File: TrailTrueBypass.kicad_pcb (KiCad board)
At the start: 2 copper layers, 38.1 x 22.6 mm, 53 parts, among them J1 Conn_01x05_Pin, J2 Conn_01x05_Pin, J3 Conn_02x03_Top_Bottom, K1 G6S-2, K2 G6S-2, K3 G6S-2, Q1 2N3904, Q2 2N3904, Q3 2N3904, U1 Opamp_Quad, U2 MC78L05_SOT89, U3 PIC12F675-xP

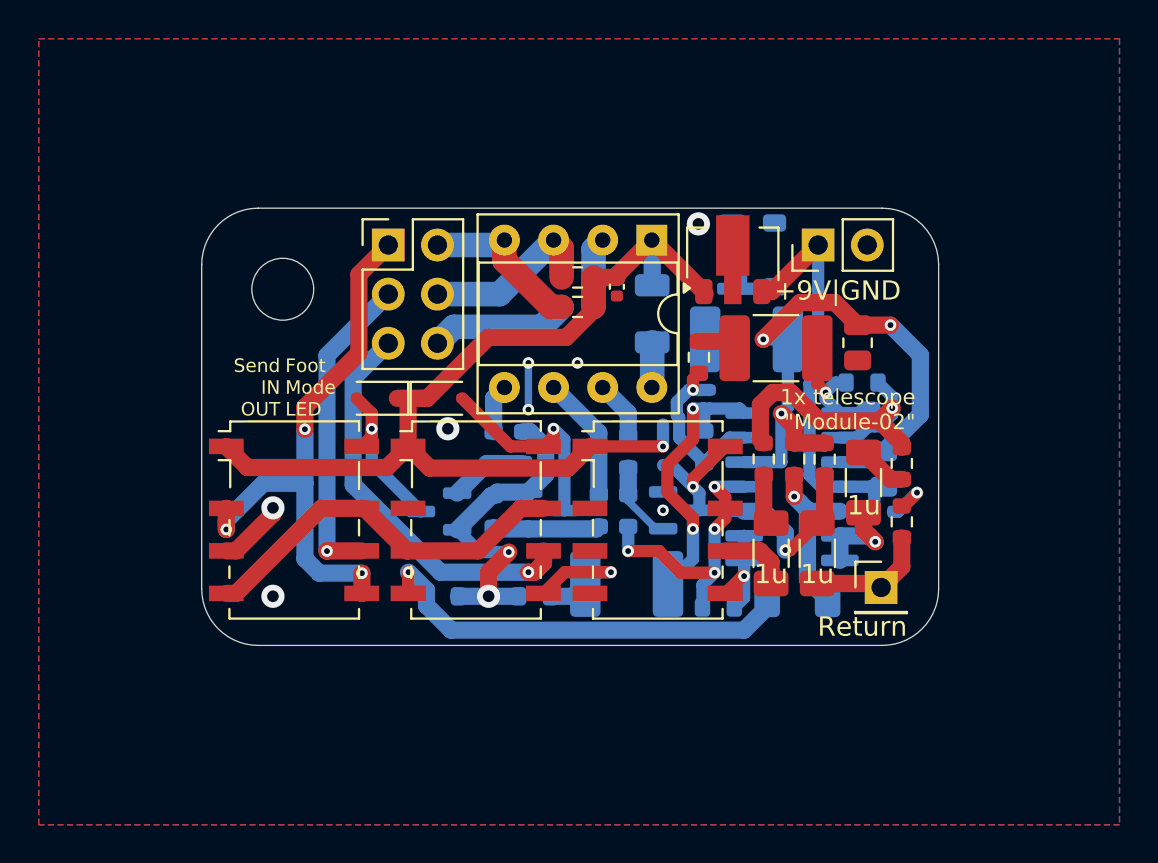
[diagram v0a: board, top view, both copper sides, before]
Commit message: update: pcbファイルを修正
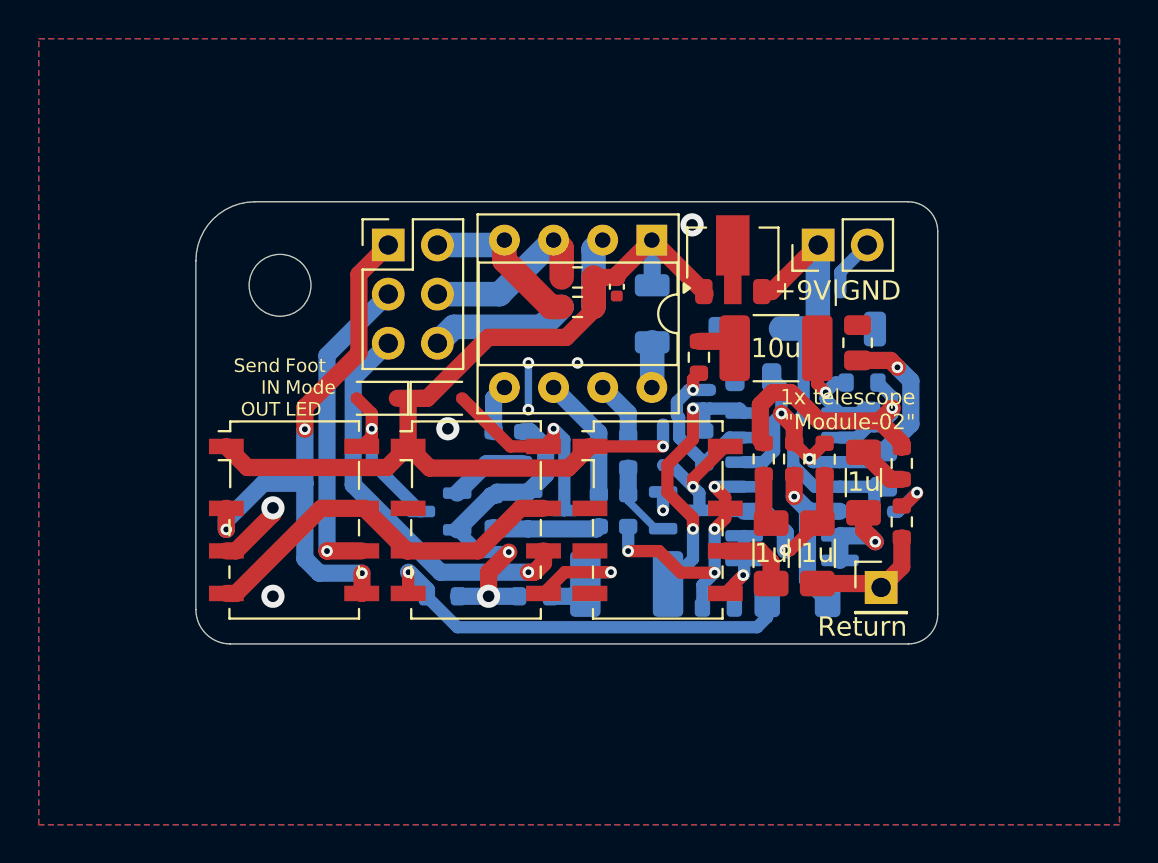
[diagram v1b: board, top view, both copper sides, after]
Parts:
- C14: value 47u -> 22u; footprint Capacitor_SMD:C_1812_4532Metric_Pad1.57x3.40mm_HandSolder -> Capacitor_SMD:C_0805_2012Metric
- C9: value 22u -> 47u; footprint Capacitor_SMD:C_0805_2012Metric -> Capacitor_SMD:C_1206_3216Metric
- moved C9 7.42 mm to (87.5, 31.5), turned to 0 degrees
- moved C11 5.14 mm to (86.7, 29.6), turned to 0 degrees
- moved D4 4.03 mm to (82.4, 31.4), turned to 180 degrees
- moved C14 1.99 mm to (82.7, 34.0)
- moved H1 0.25 mm to (58.2, 29.2)
- turned R19 to -90 degrees
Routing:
- net Vb: track 31.4 -> 21.6 mm
- net GND: track 43.4 -> 50.2 mm
- net +9V: track 28.0 -> 24.3 mm
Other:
- board size 38.1 x 22.6 mm -> 38.4 x 22.9 mm
